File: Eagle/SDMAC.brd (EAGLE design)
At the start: 81.3 x 45.9 mm, 3 parts, among them IC1 SUPER_DMAC_THT, J1 CORTEX_DEBUG_PTH, U1 XC95288XL-10TQG144C

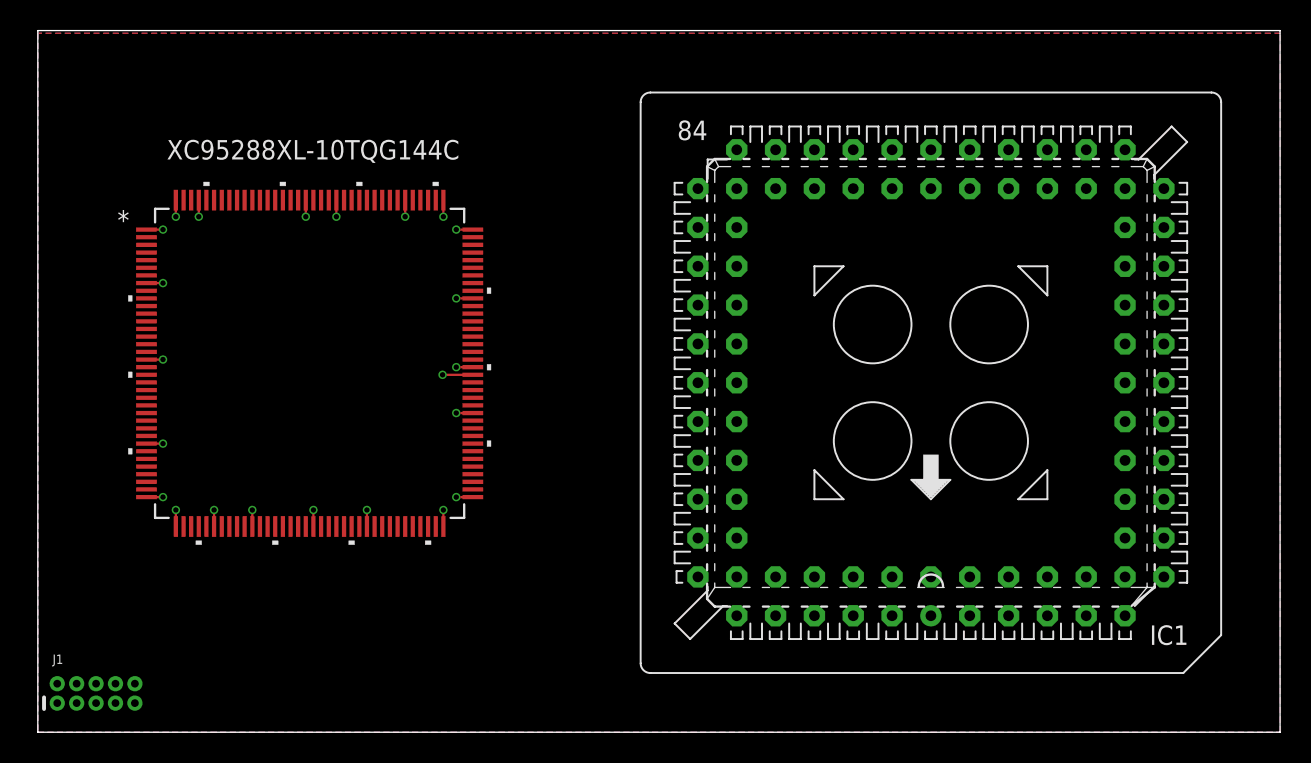
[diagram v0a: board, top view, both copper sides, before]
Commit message: added remaaining singnals to top and renamed them to be more consistant.
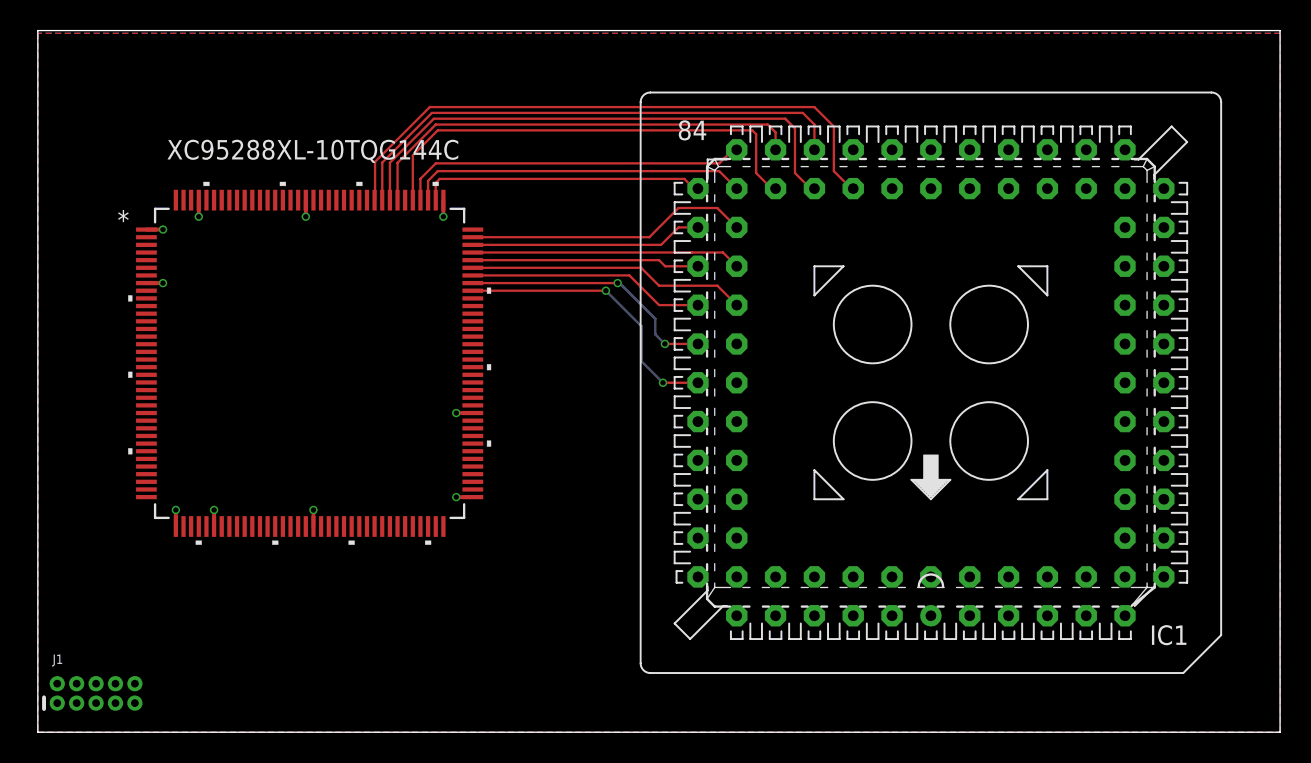
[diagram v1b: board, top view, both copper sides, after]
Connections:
- new net !AS: IC1.38
- new net !CS: IC1.45
- new net !DS: IC1.39
- new net !RST: IC1.46
- new net R!W: IC1.37
- net P_DATA0: now also U1.118
- net P_DATA1: now also U1.117
- net P_DATA10: now also U1.104
- net P_DATA11: now also U1.105
- net P_DATA12: now also U1.102
- net P_DATA13: now also U1.103
- net P_DATA14: now also U1.101
- net P_DATA15: now also U1.100
- net P_DATA2: now also U1.116
- net P_DATA3: now also U1.115
- net P_DATA4: now also U1.113
- net P_DATA5: now also U1.112
- net P_DATA6: now also U1.110
- net P_DATA7: now also U1.111
- net P_DATA8: now also U1.106
- net P_DATA9: now also U1.107
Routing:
- net P_DATA0: track 0.00 -> 39.2 mm
- net P_DATA2: track 0.00 -> 35.0 mm
- net P_DATA1: track 0.00 -> 34.0 mm
- net P_DATA4: track 0.00 -> 30.4 mm
- net P_DATA3: track 0.00 -> 29.6 mm
- net P_DATA5: track 0.00 -> 22.9 mm
- net P_DATA7: track 0.00 -> 22.2 mm
- net P_DATA6: track 0.00 -> 18.7 mm
- net P_DATA9: track 0.00 -> 18.6 mm
- net P_DATA15: track 0.00 -> 18.6 mm, vias 0 -> 2
- net P_DATA13: track 0.00 -> 18.3 mm
- net P_DATA11: track 0.00 -> 17.6 mm
- net P_DATA14: track 0.00 -> 17.0 mm, vias 0 -> 2
- net P_DATA12: track 0.00 -> 15.5 mm
- net P_DATA8: track 0.00 -> 15.2 mm
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
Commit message: More updates
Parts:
- added C1, C2: 10uF, Capacitor:CAPC2012X110
- added U2: NCP1117ST33T3G, IC:SOT-223
- moved J1 16.0 mm to (38.6, 17.9), turned to 180 degrees
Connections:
- net GND: now also C1.2, C2.2, U2.1
- net VCC3.3: now also C2.1, U2.2, U2.4
- net VCC5: now also C1.1, U2.3
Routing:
- net VCC5: track 0.00 -> 31.4 mm, vias 0 -> 1
- net VCC3.3: track 10.8 -> 28.8 mm, vias 10 -> 12
- net TCK: track 0.00 -> 13.9 mm, vias 0 -> 2
- net TMS: track 0.00 -> 10.2 mm, vias 0 -> 2
- net P_DATA6: track 18.7 -> 22.4 mm
- net P_DATA7: track 22.2 -> 25.6 mm
- net P_DATA5: track 22.9 -> 24.8 mm
- net P_DATA0: track 39.2 -> 40.4 mm
- net P_DATA1: track 34.0 -> 35.2 mm
- net P_DATA2: track 35.0 -> 36.1 mm
- net P_DATA3: track 29.6 -> 30.5 mm

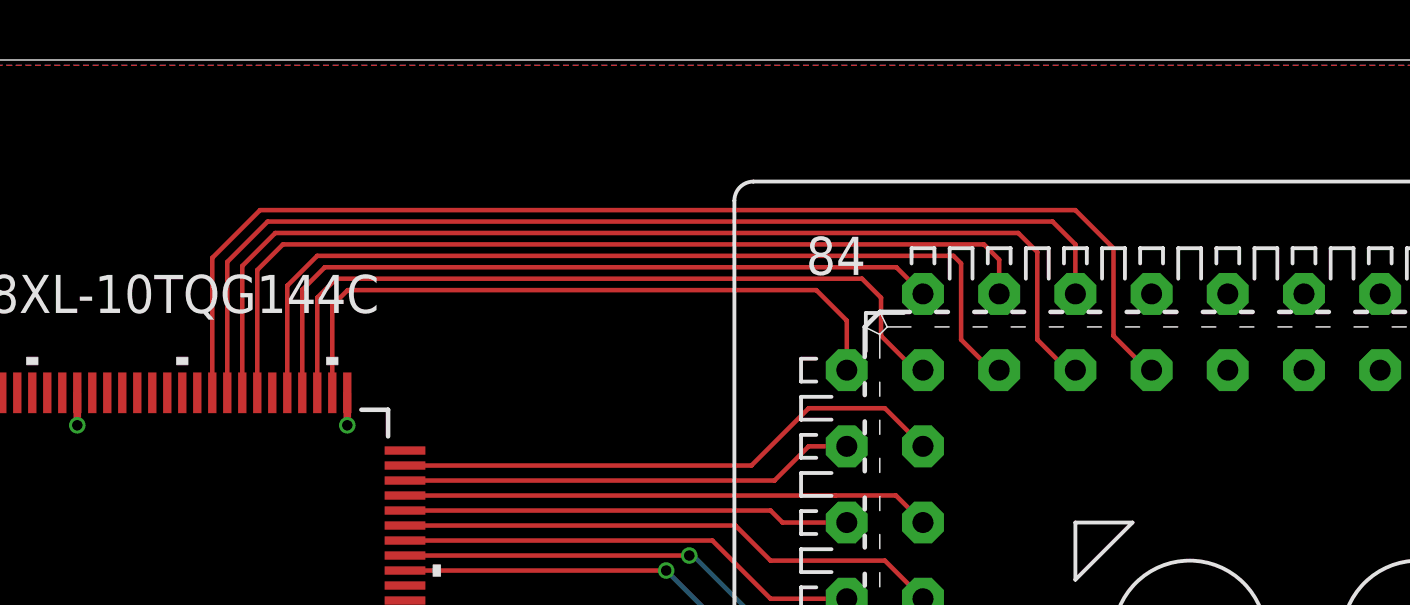
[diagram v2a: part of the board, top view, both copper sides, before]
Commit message: setting pin assignments
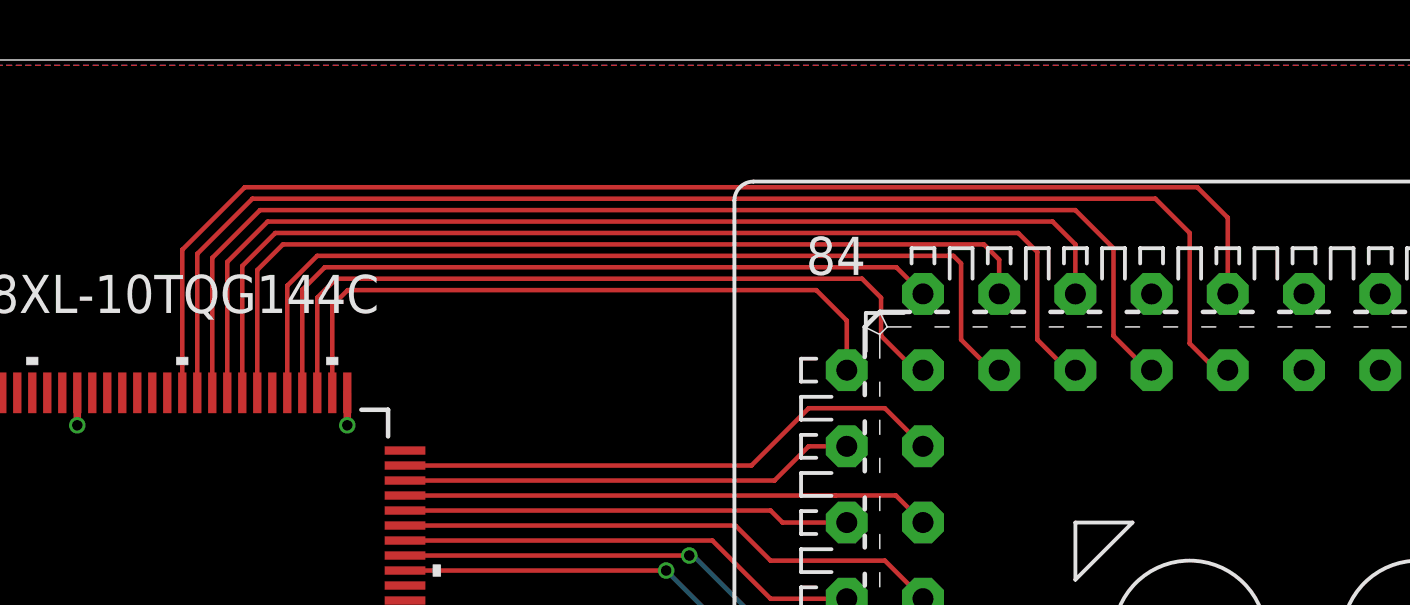
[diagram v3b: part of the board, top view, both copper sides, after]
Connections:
- net !CS: now also U1.120
- net !RST: now also U1.119
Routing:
- net !RST: track 0.00 -> 44.3 mm
- net !CS: track 0.00 -> 43.4 mm
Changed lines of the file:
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@@
 <drawing>
 <settings>
-<setting alwaysvectorfont="yes"/>
+<setting alwaysvectorfont="no"/>
 <setting verticaltext="up"/>
 </settings>
@@
 <signal name="!RST">
 <contactref element="IC1" pad="46"/>
+<contactref element="U1" pad="119"/>
+<wire x1="74.93" y1="48.26" x2="74.549" y2="48.26" width="0.1524" layer="1"/>
+<wire x1="74.549" y1="48.26" x2="73.66" y2="49.149" width="0.1524" layer="1"/>
+<wire x1="73.66" y1="52.832" x2="72.517" y2="53.975" width="0.1524" layer="1"/>
+<wire x1="72.517" y1="53.975" x2="42.418" y2="53.975" width="0.1524" layer="1"/>
+<wire x1="40.58" y1="52.137" x2="40.58" y2="47.50435" width="0.1524" layer="1"/>
+<wire x1="73.66" y1="49.149" x2="73.66" y2="52.832" width="0.1524" layer="1"/>
+<wire x1="42.418" y1="53.975" x2="40.58" y2="52.137" width="0.1524" layer="1"/>
 </signal>
 <signal name="!DS">
@@
 <signal name="!CS">
 <contactref element="IC1" pad="45"/>
+<contactref element="U1" pad="120"/>
+<wire x1="40.08" y1="47.50435" x2="40.08" y2="52.272" width="0.1524" layer="1"/>
+<wire x1="40.08" y1="52.272" x2="42.164" y2="54.356" width="0.1524" layer="1"/>
+<wire x1="42.164" y1="54.356" x2="73.914" y2="54.356" width="0.1524" layer="1"/>
+<wire x1="73.914" y1="54.356" x2="74.93" y2="53.34" width="0.1524" layer="1"/>
+<wire x1="74.93" y1="53.34" x2="74.93" y2="50.8" width="0.1524" layer="1"/>
 </signal>
 </signals>

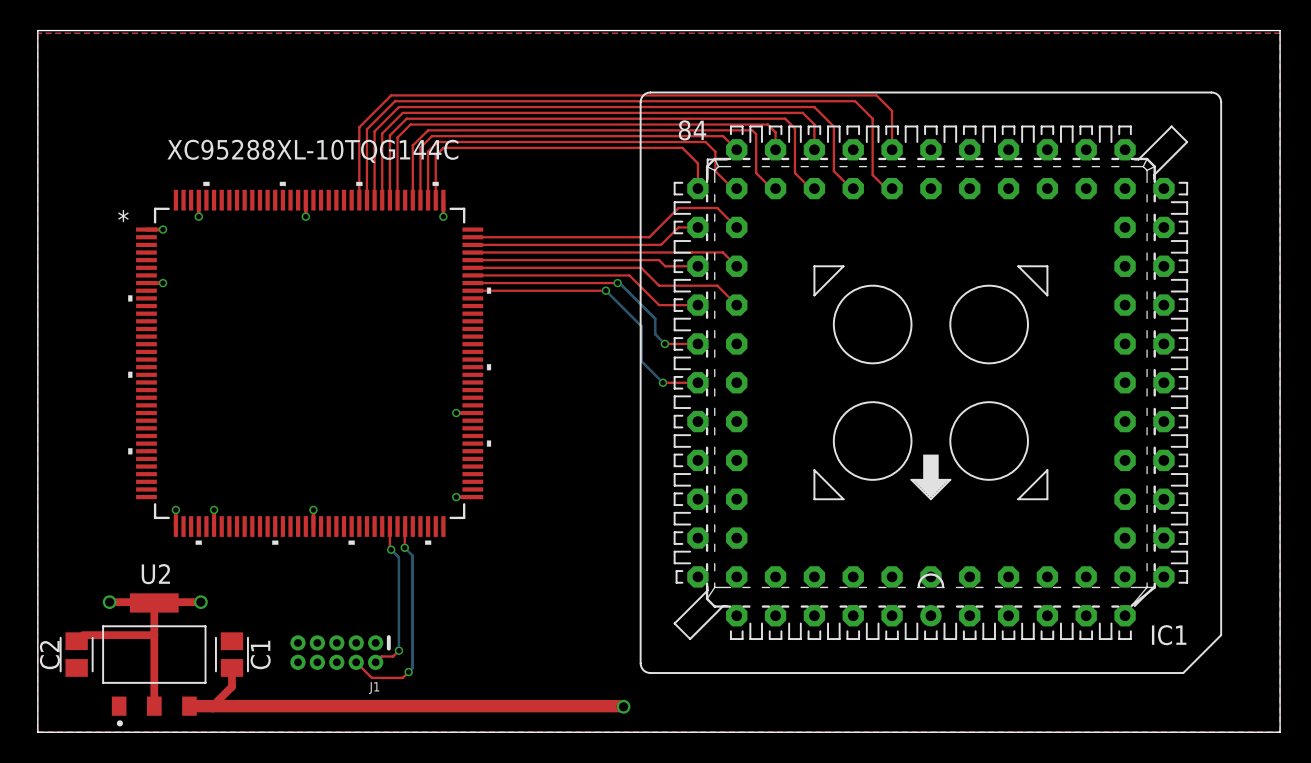
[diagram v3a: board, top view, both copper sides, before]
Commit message: Routed more singnals and added example timing diagam to SDMAC.md
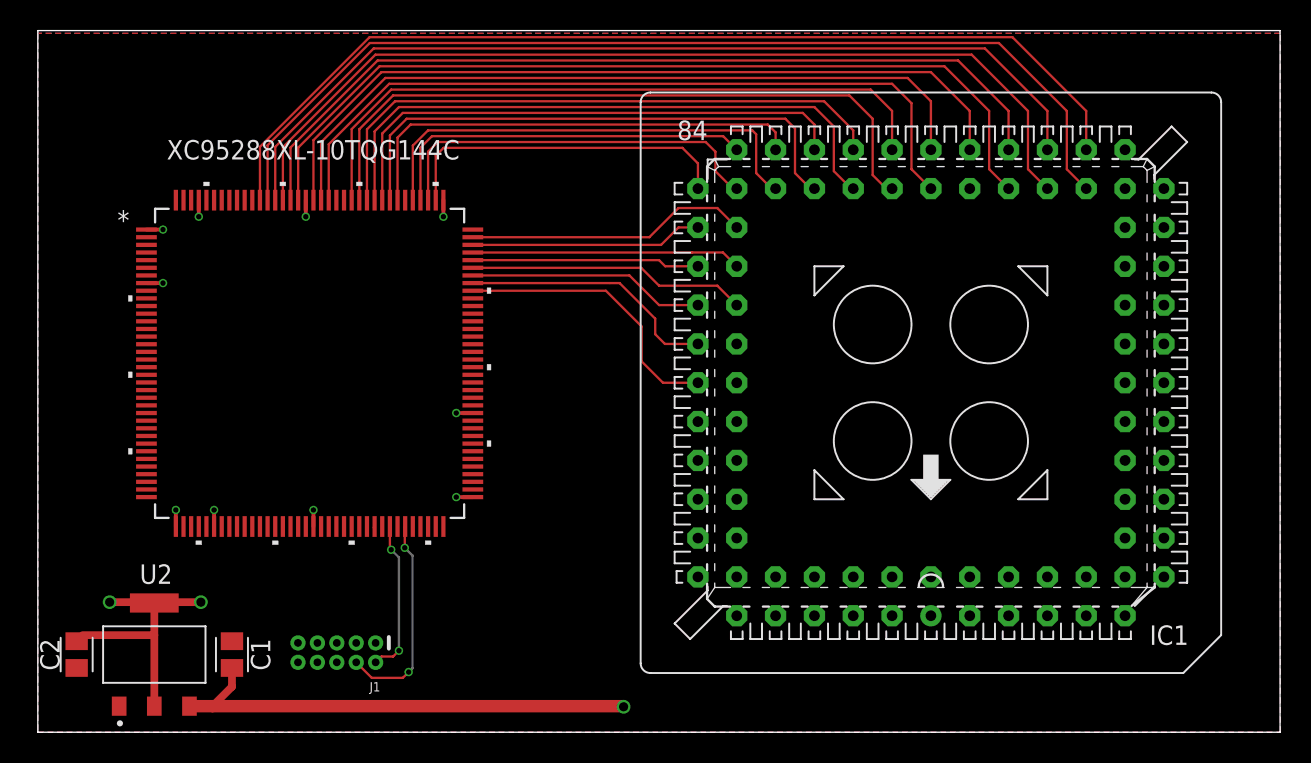
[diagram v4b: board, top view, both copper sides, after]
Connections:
- new net !BERR: IC1.47, U1.119
- new net !BG: IC1.82
- new net !BGACK: IC1.83
- new net !BR: IC1.81
- new net !CSS: IC1.67
- new net !CSX0: IC1.70
- new net !CSX1: IC1.71
- new net !DACK: IC1.66
- new net !DMAEN: IC1.75
- new net !DREQ: IC1.65
- new net !DSACK0: IC1.41, U1.126
- new net !DSACK1: IC1.40, U1.128
- new net !INT2: IC1.35, U1.133
- new net !IOR: IC1.69
- new net !IORDY: IC1.72
- new net !IOW: IC1.68
- new net !STERM: IC1.43, U1.125
- new net INC_ADD: IC1.74
- new net INTA: IC1.73
- new net INTB: IC1.34
- new net SIZ1: IC1.36, U1.132
- net !AS: now also U1.130
- net !CS: now also U1.121; no longer U1.120
- net !DS: now also U1.129
- net !RST: now also U1.120; no longer U1.119
- net CLK: now also U1.124
- net R!W: now also U1.131
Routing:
- net SIZ1: track 0.00 -> 66.1 mm
- net !INT2: track 0.00 -> 65.0 mm
- net !AS: track 0.00 -> 61.8 mm
- net R!W: track 0.00 -> 60.9 mm
- net !DSACK1: track 0.00 -> 57.7 mm
- net !DS: track 0.00 -> 56.7 mm
- net !DSACK0: track 0.00 -> 52.3 mm
- net CLK: track 0.00 -> 50.1 mm
- net !STERM: track 0.00 -> 49.2 mm
- net !BERR: track 0.00 -> 39.3 mm
- net !RST: track 44.3 -> 45.1 mm
- net !CS: track 43.4 -> 44.2 mm
- net P_DATA15: vias 2 -> 0
- net P_DATA14: vias 2 -> 0

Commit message: Finished Initial Routing of signals in PCB design
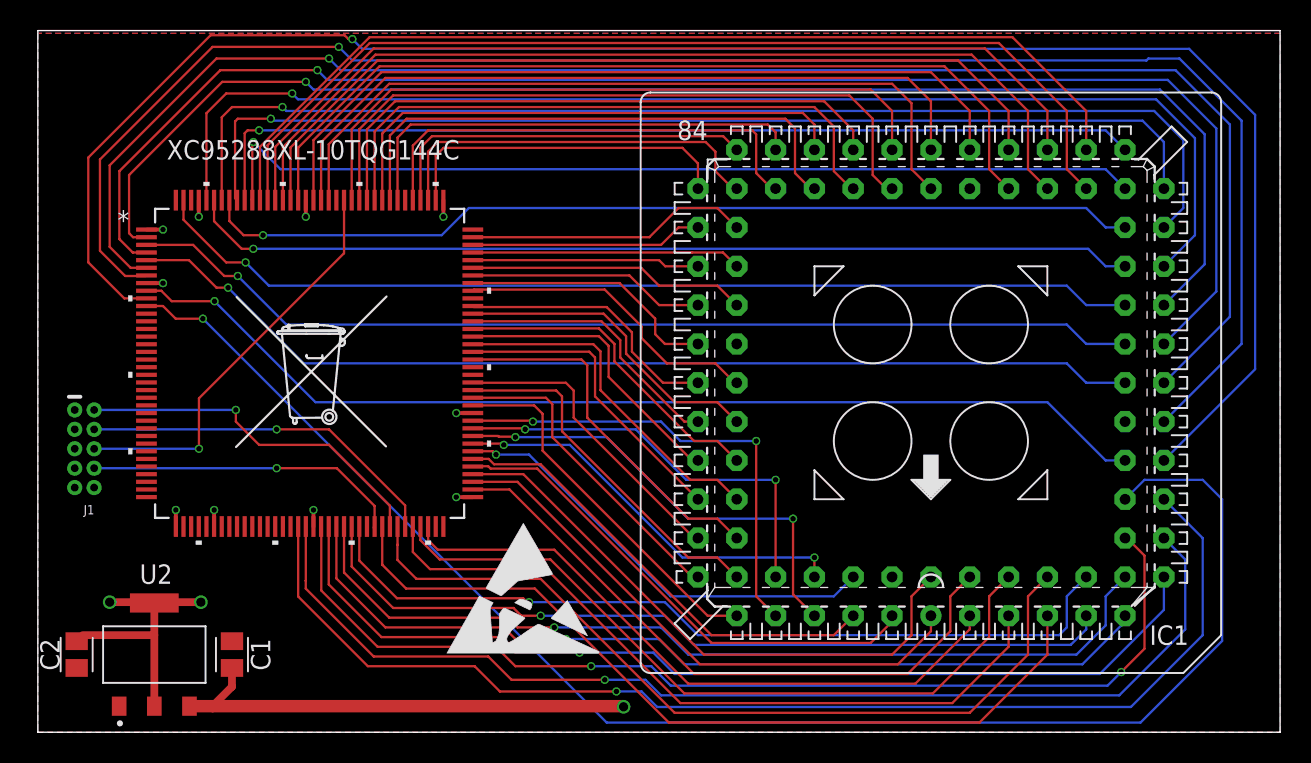
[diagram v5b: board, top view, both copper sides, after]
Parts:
- added U$1: (no value), logo:ESD_10.00
- added U$2: (no value), logo:TONNE_10.00
- moved J1 21.2 mm to (22.1, 31.2), turned to 270 degrees
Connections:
- net !BG: now also U1.79
- net !BGACK: now also U1.77
- net !BR: now also U1.78
- net !CSS: now also U1.97
- net !CSX0: now also U1.92
- net !CSX1: now also U1.93
- net !DACK: now also U1.96
- net !DMAEN: now also U1.85
- net !DREQ: now also U1.100
- net !IOR: now also U1.95
- net !IORDY: now also U1.88
- net !IOW: now also U1.94
- net CPU_ADDR2: now also U1.87
- net CPU_ADDR3: now also U1.83
- net CPU_ADDR4: now also U1.82
- net CPU_ADDR5: now also U1.81
- net CPU_ADDR6: now also U1.80
- net CPU_DATAD0: now also U1.75
- net CPU_DATAD1: now also U1.76
- net CPU_DATAD10: now also U1.58
- net CPU_DATAD11: now also U1.57
- net CPU_DATAD12: now also U1.59
- net CPU_DATAD13: now also U1.54
- net CPU_DATAD14: now also U1.56
- net CPU_DATAD15: now also U1.53
- net CPU_DATAD16: now also U1.11
- net CPU_DATAD17: now also U1.10
- net CPU_DATAD18: now also U1.9
- net CPU_DATAD19: now also U1.7
- net CPU_DATAD2: now also U1.70
- net CPU_DATAD20: now also U1.6
- net CPU_DATAD21: now also U1.5
- net CPU_DATAD22: now also U1.4
- net CPU_DATAD23: now also U1.3
- net CPU_DATAD24: now also U1.2
- net CPU_DATAD25: now also U1.143
- net CPU_DATAD26: now also U1.140
- net CPU_DATAD27: now also U1.139
- net CPU_DATAD28: now also U1.138
- net CPU_DATAD29: now also U1.137
- net CPU_DATAD3: now also U1.74
- net CPU_DATAD30: now also U1.136
- net CPU_DATAD31: now also U1.135
- net CPU_DATAD4: now also U1.68
- net CPU_DATAD5: now also U1.69
- net CPU_DATAD6: now also U1.64
- net CPU_DATAD7: now also U1.66
- net CPU_DATAD8: now also U1.60
- net CPU_DATAD9: now also U1.61
- net INC_ADD: now also U1.86
- net INTA: now also U1.91
- net INTB: now also U1.134
- net P_DATA15: now also U1.98; no longer U1.100
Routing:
- net CPU_DATAD17: track 0.00 -> 118.5 mm, vias 0 -> 1
- net CPU_DATAD19: track 0.00 -> 111.3 mm, vias 0 -> 1
- net CPU_DATAD20: track 0.00 -> 104.9 mm, vias 0 -> 1
- net CPU_DATAD16: track 0.00 -> 100.5 mm, vias 0 -> 1
- net CPU_DATAD22: track 0.00 -> 98.2 mm, vias 0 -> 1
- net CPU_DATAD24: track 0.00 -> 91.6 mm, vias 0 -> 1
- net CPU_DATAD26: track 0.00 -> 81.3 mm, vias 0 -> 1
- net CPU_DATAD15: track 0.00 -> 78.6 mm, vias 0 -> 1
- net CPU_DATAD28: track 0.00 -> 75.7 mm, vias 0 -> 1
- net CPU_DATAD13: track 0.00 -> 72.8 mm, vias 0 -> 1
- net CPU_DATAD30: track 0.00 -> 69.7 mm, vias 0 -> 1
- net CPU_DATAD14: track 0.00 -> 69.5 mm, vias 0 -> 2
- net CPU_DATAD18: track 0.00 -> 68.6 mm, vias 0 -> 1
- net CPU_DATAD21: track 0.00 -> 67.3 mm, vias 0 -> 1
- net CPU_DATAD23: track 0.00 -> 66.7 mm, vias 0 -> 1
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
